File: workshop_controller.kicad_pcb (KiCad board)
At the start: 2 copper layers, 170 x 90 mm, 33 parts, among them J1 Conn_02x10_Odd_Even, J2 Conn_02x10_Odd_Even, J3 AudioJack3, J4 Micro_SD_Card, J5 Conn_02x25_Odd_Even, SW1 SW_Push, SW2 SW_Push, SW3 SW_Push, SW4 SW_Push, U1 MPU-9250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

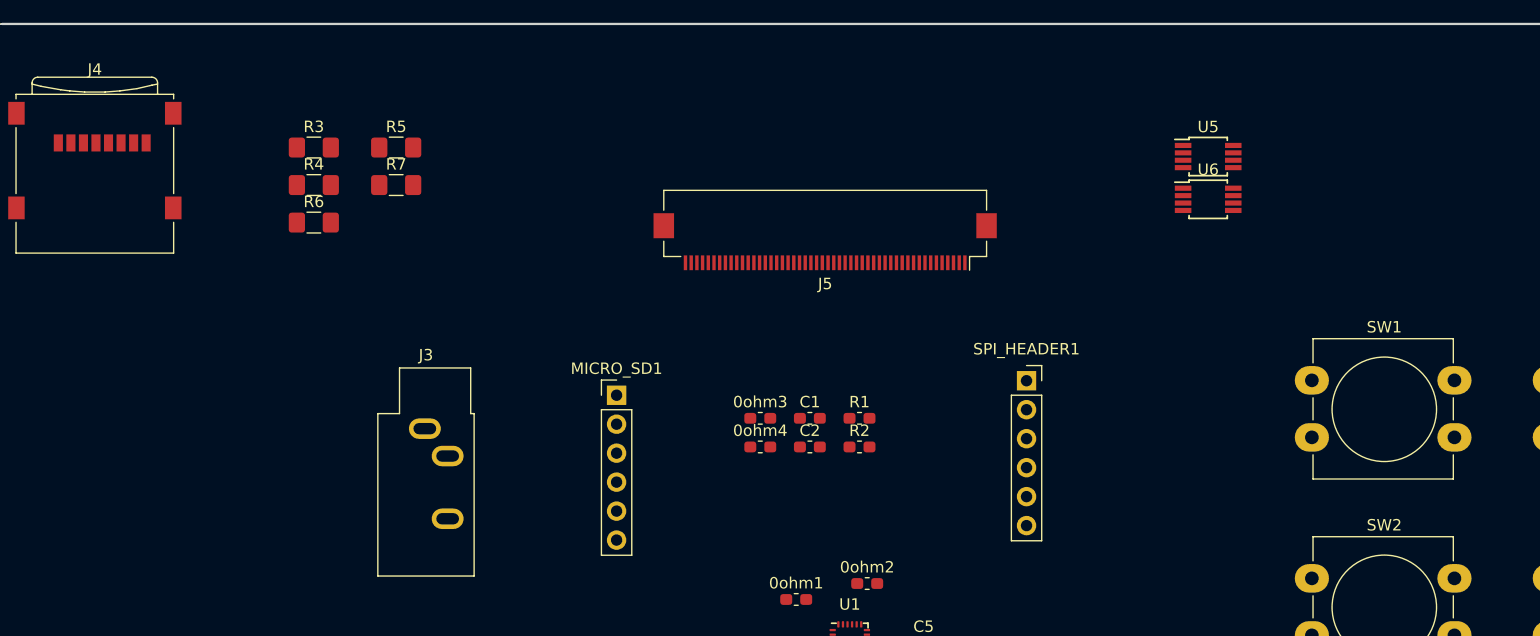
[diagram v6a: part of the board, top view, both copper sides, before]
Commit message: Add microphone circuit
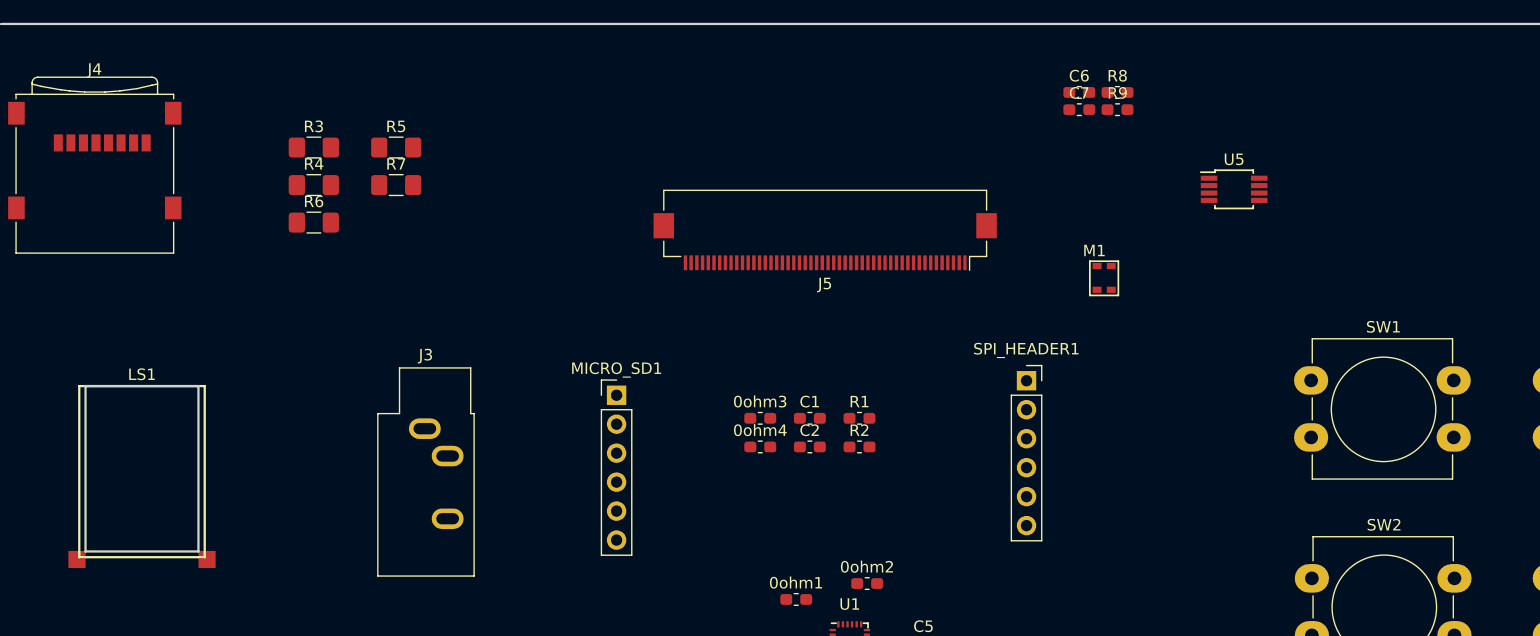
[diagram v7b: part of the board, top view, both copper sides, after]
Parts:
- removed U6: LM358, Package_SO:MSOP-8_3x3mm_P0.65mm
- added C6: 0.1µF, Capacitor_SMD:C_0603_1608Metric_Pad1.05x0.95mm_HandSolder, F.Cu at (174.4, 56.0)
- added C7: 0.1µF, Capacitor_SMD:C_0603_1608Metric_Pad1.05x0.95mm_HandSolder, F.Cu at (174.4, 57.5)
- added LS1: Speaker, Hackheim_logo:Speaker_SMD_CUI, F.Cu at (92.2, 81.8)
- added M1: Microphone4, Hackheim_logo:CMM-3125AT-42316-TR, F.Cu at (175.8, 71.0)
- added R8: ?ohm, Resistor_SMD:R_0603_1608Metric_Pad1.05x0.95mm_HandSolder, F.Cu at (177.8, 56.0)
- added R9: ?ohm, Resistor_SMD:R_0603_1608Metric_Pad1.05x0.95mm_HandSolder, F.Cu at (177.8, 57.5)
- moved U5 3.67 mm to (188.0, 64.5)
- moved SW1 0.07 mm to (194.8, 81.2)
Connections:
- J2 pad 6: Net-(J2-Pad6) -> /DAC25
- U5 pad 1: Net-(U5-Pad1) -> /DAC25
- U5 pad 2: Net-(U5-Pad2) -> +3V3
- U5 pad 4: (no net) -> Net-(U5-Pad4)
- U5 pad 5: (no net) -> Net-(U5-Pad5)
- U5 pad 6: (no net) -> Net-(U5-Pad6)
- U5 pad 7: (no net) -> Net-(U5-Pad7)
- U5 pad 8: (no net) -> Net-(U5-Pad8)

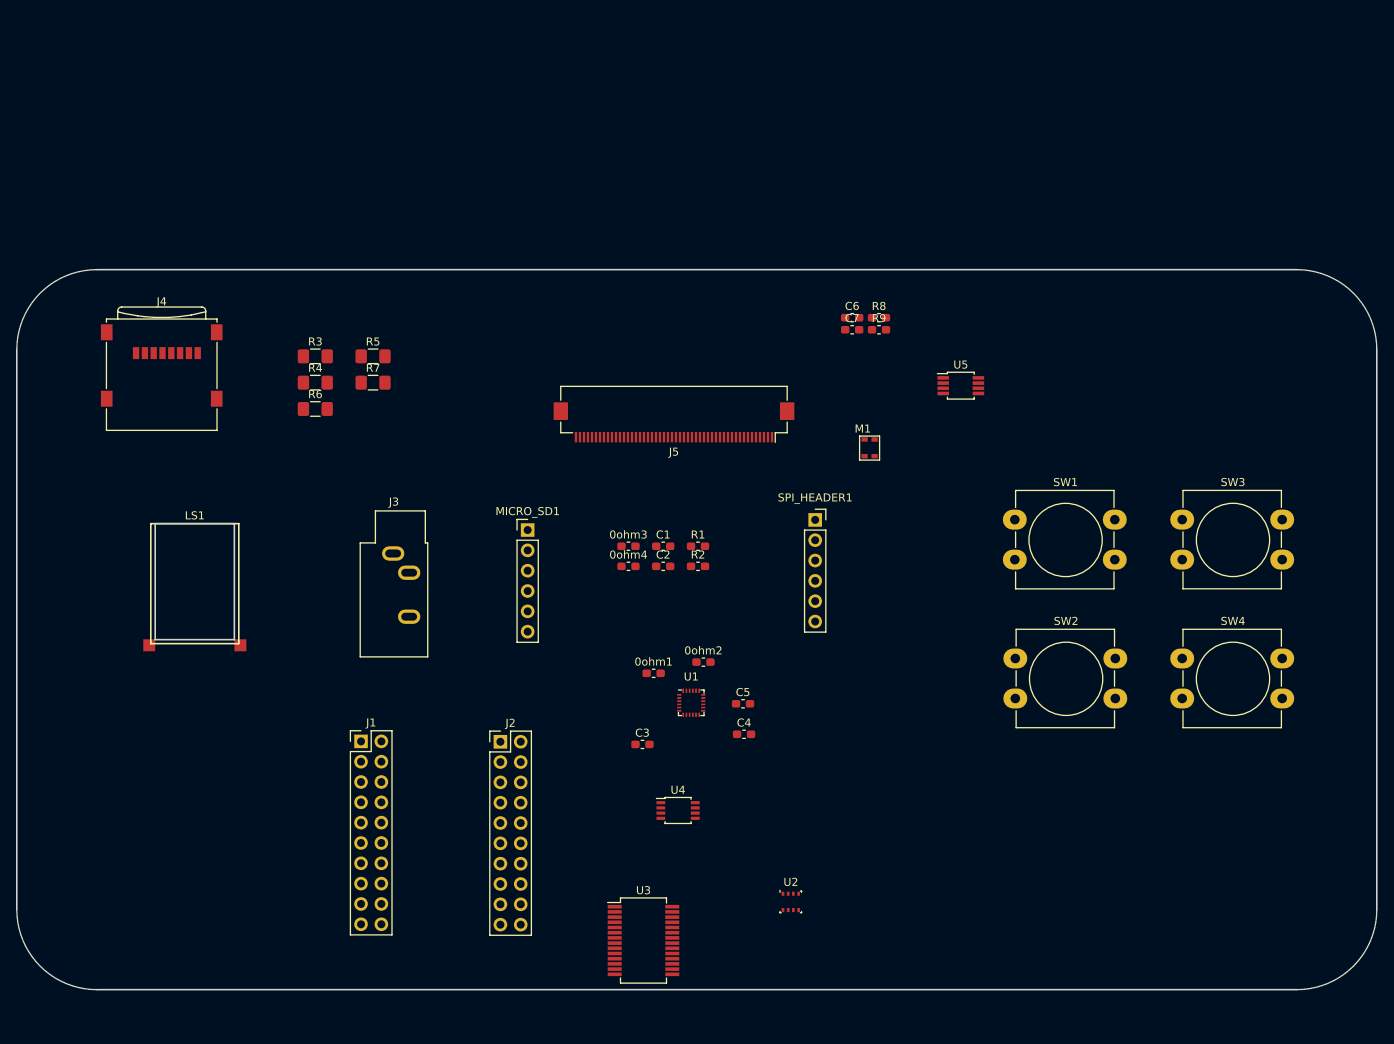
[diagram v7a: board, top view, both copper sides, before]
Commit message: Wire BME280
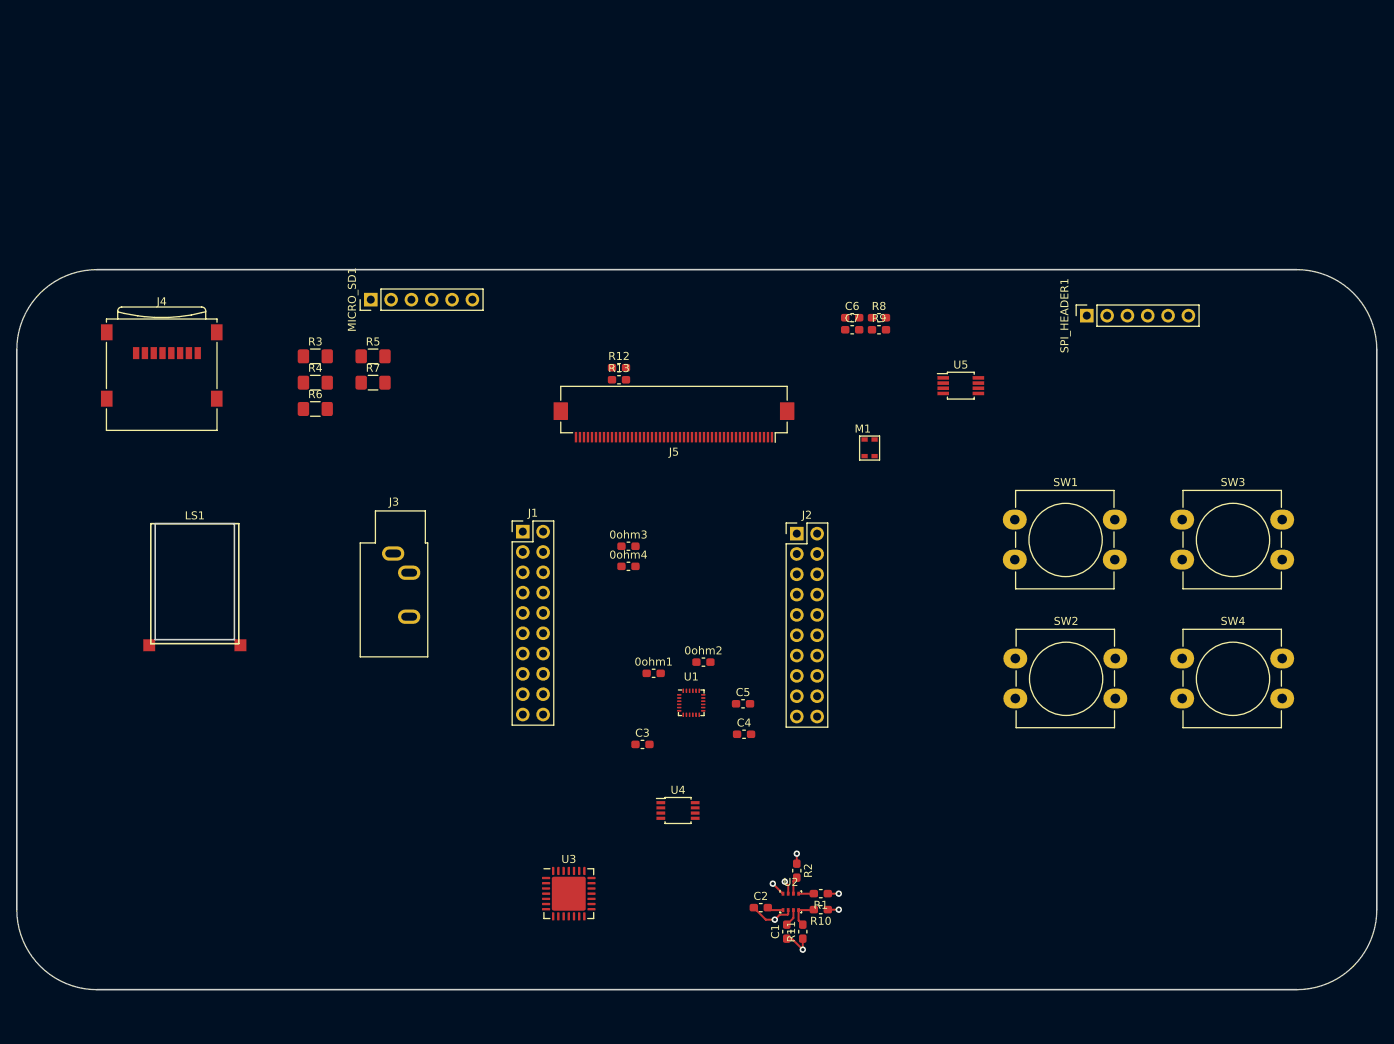
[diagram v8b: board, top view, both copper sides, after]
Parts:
- added R10: R_Small, Resistor_SMD:R_0603_1608Metric_Pad1.05x0.95mm_HandSolder, F.Cu at (170.5, 130.0)
- added R11: R_Small, Resistor_SMD:R_0603_1608Metric_Pad1.05x0.95mm_HandSolder, F.Cu at (168.2, 132.8)
- added R12: R_Small, Resistor_SMD:R_0603_1608Metric_Pad1.05x0.95mm_HandSolder, F.Cu at (145.3, 62.3)
- added R13: R_Small, Resistor_SMD:R_0603_1608Metric_Pad1.05x0.95mm_HandSolder, F.Cu at (145.3, 63.8)
- U3: value MCP23S17_SS -> MCP23017_ML; footprint Package_SO:SSOP-28_5.3x10.2mm_P0.65mm -> Package_DFN_QFN:QFN-28-1EP_6x6mm_P0.65mm_EP4.25x4.25mm
- moved C1 50.6 mm to (166.2, 132.8), turned to 90 degrees
- moved R1 46.1 mm to (170.5, 128.0), turned to 180 degrees
- moved J2 45.3 mm to (167.5, 83.0)
- moved C2 44.4 mm to (163.0, 129.8)
- moved SPI_HEADER1 42.5 mm to (203.8, 55.8), turned to 90 degrees
- moved R2 40.0 mm to (167.5, 125.1), turned to 270 degrees
- moved MICRO_SD1 34.8 mm to (114.2, 53.8), turned to 90 degrees
- moved J1 33.1 mm to (133.2, 82.8)
- moved U3 11.0 mm to (139.0, 128.0)
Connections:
- U1 pad 9: Net-(0ohm1-Pad2) -> Net-(R12-Pad2)
- U2 pad 5: Net-(0ohm3-Pad2) -> Net-(R10-Pad2)
- U3 pad 5: Net-(U3-Pad5) -> +3V3
- U3 pad 8: Net-(U3-Pad8) -> /I2C_SCK
- U3 pad 9: Net-(U3-Pad9) -> /I2C_SDA
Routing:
- net GND: track 0.00 -> 11.5 mm, vias 0 -> 3
- net +3V3: track 0.00 -> 5.68 mm, vias 0 -> 4
- net Net-(R10-Pad2): track 0.00 -> 3.96 mm
- net /I2C_SDA: track 0.00 -> 2.18 mm
- net Net-(C1-Pad2): track 0.00 -> 2.16 mm
- net Net-(C2-Pad2): track 0.00 -> 2.03 mm
- net /I2C_SCK: track 0.00 -> 1.90 mm
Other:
- copper layers 2 -> 4
